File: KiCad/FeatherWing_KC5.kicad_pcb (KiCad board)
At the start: 2 copper layers, 50.8 x 71.1 mm, 38 parts, among them J1 feather long, J2 feather short, J5 AudioJack4, U1 DRA818V, U2 DRA818U, U3 LM4810

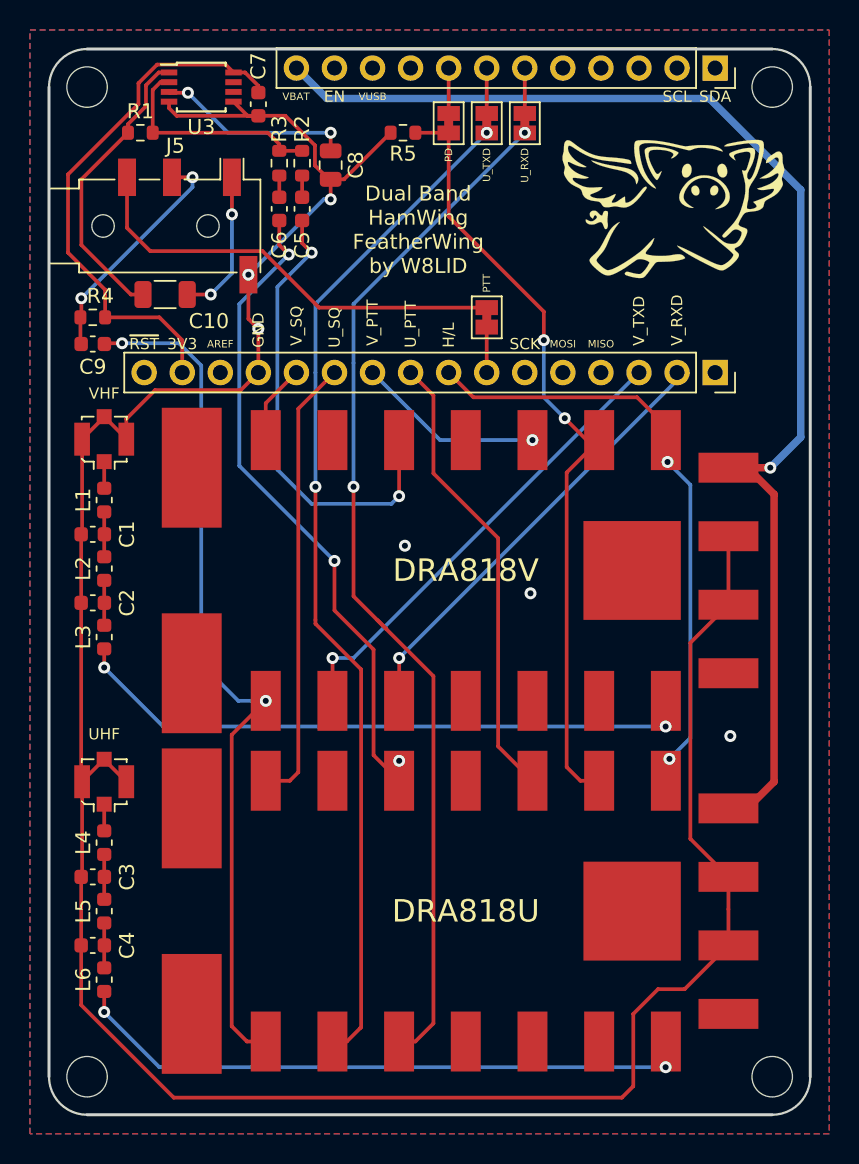
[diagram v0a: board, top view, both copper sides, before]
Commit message: KiCad Updates
Imported project to KiCad 8.0
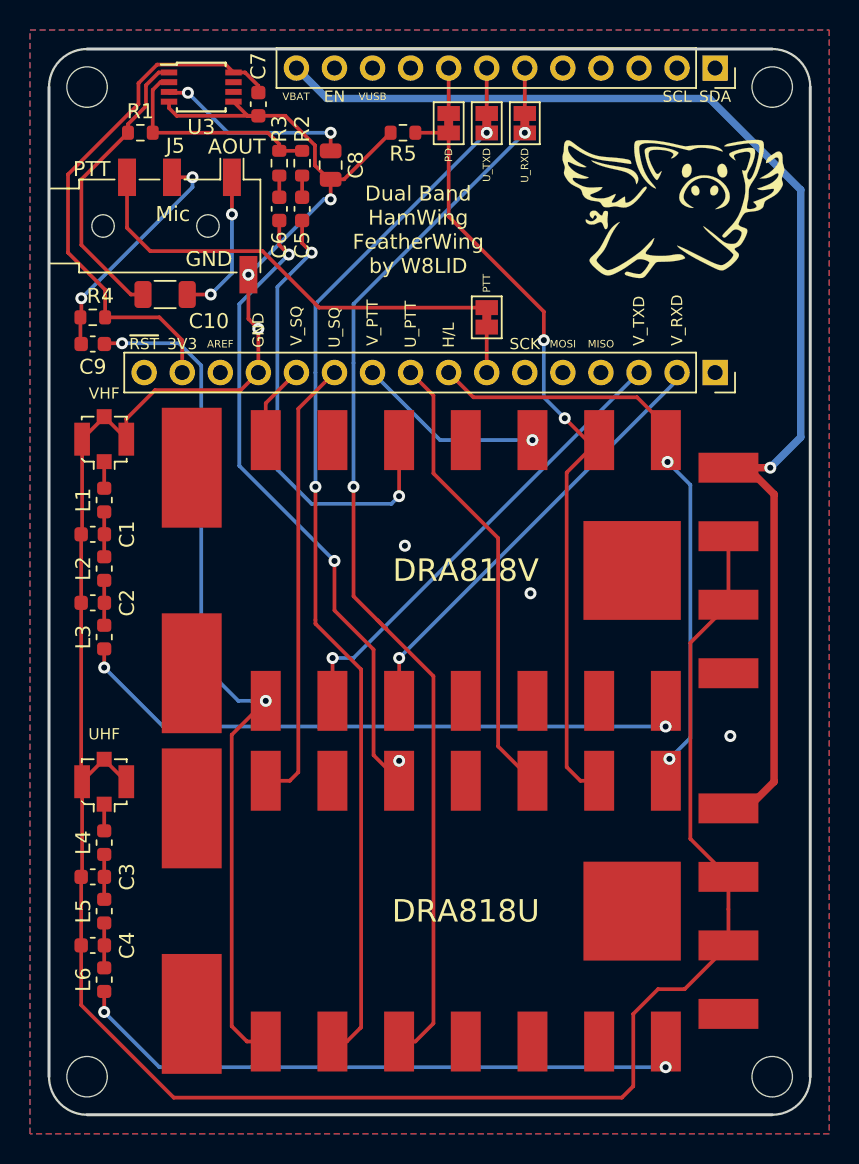
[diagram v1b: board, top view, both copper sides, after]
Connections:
- net /~RST renamed /~{RST}
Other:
- net class Default removed
- board text added: "AOUT"
- board text added: "Mic"
- board text added: "~{RST}"
- board text removed: "~RST"
